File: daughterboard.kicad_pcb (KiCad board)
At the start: 2 copper layers, 72.2 x 85.7 mm, 64 parts, among them J1 MotorA, J10 J, J11 J, J12 J, J13 J, J14 J, J15 J, J16 J, J17 J, J18 J, J19 J, J2 MotorB, J20 J, J21 J, J22 J, J23 J, J24 J, J25 J, J26 J, J27 J, J28 J, J29 J, J3 BARREL_JACK, J30 J, J31 J, J32 J, J33 J, J34 J, J35 J, J36 J, J37 J, J38 J, J39 J, J4 Debug, J40 J, J41 J, J42 J, J43 J, J44 J, J5 QTR-8A, J6 J, J7 J, J8 J, J9 J, SW1 Reset, U1 LD1117S33CTR, U2 TB6612FNG, U3 EFM32G230F128

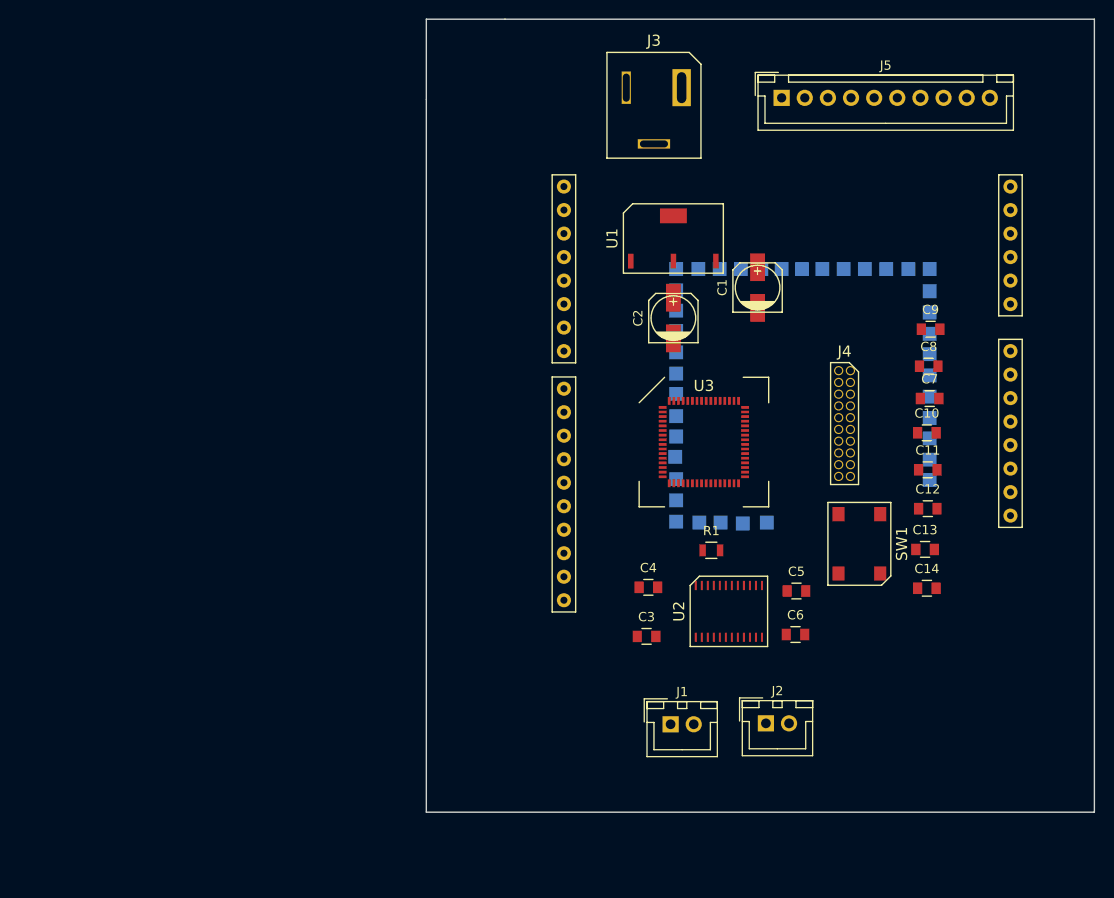
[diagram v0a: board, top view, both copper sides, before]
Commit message: Update PCB to reflect schematic changes
Since we reannotated just about the entire schematic it was easier
to just clear the entire pcb and layout the components again.

Moved the QR8 to the bottom and TB6612 to the top, since it made
more sense wrt the pinout of the EFM32.
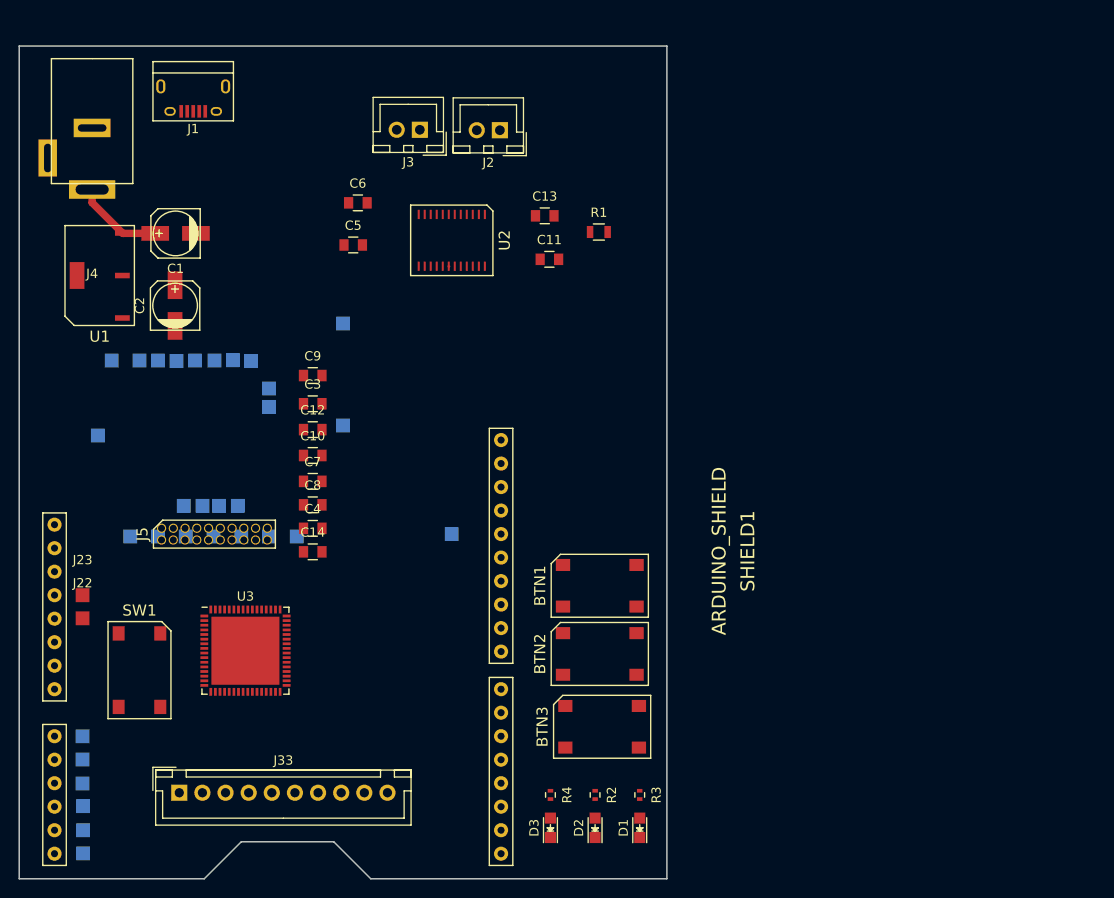
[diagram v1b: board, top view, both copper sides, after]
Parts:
- removed J40, J41, J42, J43, J44: J, Measurement_Points:Measurement_Point_Square-SMD-Pad_Small
- added BTN1: Button, footprints:SW-4, F.Cu at (126.7, 116.3)
- added BTN2: Button, footprints:SW-4, F.Cu at (126.7, 123.7)
- added BTN3: Button, footprints:SW-4, F.Cu at (127.0, 131.6)
- added D1: LED, LEDs:LED_0805, F.Cu at (131.1, 142.5)
- added D2: LED, LEDs:LED_0805, F.Cu at (126.2, 142.5)
- added D3: LED, LEDs:LED_0805, F.Cu at (121.4, 142.5)
- added R2: R, Resistors_SMD:R_0402, F.Cu at (126.2, 138.9)
- added R3: R, Resistors_SMD:R_0402, F.Cu at (131.1, 138.9)
- added R4: R, Resistors_SMD:R_0402, F.Cu at (121.4, 138.9)
- J1: value MotorA -> USB_OTG; footprint Connectors_JST:JST_XH_B02B-XH-A_02x2.50mm_Straight -> Connect:USB_Micro-B
- J2: value MotorB -> MotorA
- J22, J23: moved to F.Cu
- J3: value BARREL_JACK -> MotorB; footprint footprints:BarrelJack -> Connectors_JST:JST_XH_B02B-XH-A_02x2.50mm_Straight
- J33: value J -> QTR-8A; footprint Measurement_Points:Measurement_Point_Square-SMD-Pad_Small -> Connectors_JST:JST_XH_B10B-XH-A_10x2.50mm_Straight; moved to F.Cu
- J4: value Debug -> BARREL_JACK; footprint footprints:SOIC-20 -> footprints:2.1-MM-DC-PWR
- J5: value QTR-8A -> Debug; footprint Connectors_JST:JST_XH_B10B-XH-A_10x2.50mm_Straight -> footprints:SOIC-20
- U3: footprint footprints:QFN64 -> Housings_DFN_QFN:QFN-64-1EP_9x9mm_Pitch0.5mm
- moved J18 108.4 mm to (70.9, 140.2)
- moved J17 107.9 mm to (70.9, 142.8)
- moved J16 107.3 mm to (70.9, 145.2)
- moved J19 105.9 mm to (70.8, 137.7)
- moved J20 103.5 mm to (70.8, 135.1)
- moved J21 101.4 mm to (70.8, 132.6)
- moved J22 95.9 mm to (70.8, 119.8)
- moved J23 94.6 mm to (70.8, 117.3)
- moved J25 89.9 mm to (72.5, 100.1)
- moved J28 89.3 mm to (74.0, 92.0)
- moved J4 86.2 mm to (71.9, 70.1), turned to 180 degrees
- moved J1 85.2 mm to (82.8, 63.5), turned to 180 degrees
- moved J27 84.1 mm to (79.0, 92.0)
- moved J26 81.8 mm to (81.0, 92.0)
- moved J24 79.5 mm to (83.0, 92.0)
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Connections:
- net /ADCO_CH0 renamed Net-(J5-Pad1)
- net /ADCO_CH2 renamed Net-(J5-Pad3)
- net /ADCO_CH4 renamed Net-(J5-Pad5)
- net Net-(C14-Pad1) renamed /EFM32/DCPL
- net Net-(R1-Pad1) renamed /TB6612/STBY
- J1 pad 1: /TB6612/MotorA1 -> +5V
- J1 pad 2: /TB6612/MotorA2 -> Net-(J1-Pad2)
- J10 pad 1: /PE8 -> /EFM32/PB7
- J11 pad 1: /PE9 -> /EFM32/PB8
- J12 pad 1: /PE10 -> Net-(J12-Pad1)
- J13 pad 1: /PE11 -> Net-(J13-Pad1)
- J14 pad 1: /PE12 -> Net-(J14-Pad1)
- J15 pad 1: /PE13 -> Net-(J15-Pad1)
- J16 pad 1: /PF3 -> /AD5
- J17 pad 1: /PF4 -> /AD4
- J18 pad 1: /PF5 -> /AD3
- J19 pad 1: /EFM32/PA9 -> /AD2
- J2 pad 1: /TB6612/MotorB1 -> /TB6612/MotorA1
- J2 pad 2: /TB6612/MotorB2 -> /TB6612/MotorA2
- J20 pad 1: /EFM32/PA10 -> /AD1
- J21 pad 1: /EFM32/PA15 -> /AD0
- J22 pad 1: /EFM32/PB7 -> Net-(J22-Pad1)
- J23 pad 1: /EFM32/PB8 -> Net-(J23-Pad1)
- J24 pad 1: /PB14 -> /EFM32/PE8
- J25 pad 1: /PB13 -> /EFM32/PE9
- J26 pad 1: /PB12 -> /EFM32/PE12
- J27 pad 1: /PB11 -> /EFM32/PE13
- J28 pad 1: Net-(J28-Pad1) -> /EFM32/PE14
- J29 pad 1: Net-(J29-Pad1) -> /EFM32/PE15
- J3 pad 1: +5V -> /TB6612/MotorB2
- J3 pad 2: GND -> /TB6612/MotorB1
- J30 pad 1: Net-(J30-Pad1) -> /EFM32/PF3
- J31 pad 1: Net-(J31-Pad1) -> /EFM32/PF4
- J32 pad 1: /PA0 -> /EFM32/PF5
- J33 pad 1: /PA1 -> /EFM32/ADC0_CH0
- J34 pad 1: /PA2 -> /EFM32/PA5
- J35 pad 1: /PA3 -> /EFM32/PA6
- J36 pad 1: /PA4 -> /EFM32/PB11
- J37 pad 1: /PA5 -> /EFM32/PB12
- J38 pad 1: /PA6 -> /EFM32/PB13
- J39 pad 1: Net-(J39-Pad1) -> /EFM32/PB14
- J4 pad 1: Net-(J4-Pad1) -> +5V
- J4 pad 2: +3V3 -> GND
- J4 pad 3: Net-(J4-Pad3) -> GND
- J5 pad 2: /ADCO_CH1 -> +3V3
- J5 pad 4: /ADCO_CH3 -> GND
- J5 pad 6: /ADCO_CH5 -> GND
- J5 pad 7: /ADCO_CH6 -> /EFM32/PF1
- J5 pad 8: /ADCO_CH7 -> GND
- J5 pad 9: +3V3 -> /EFM32/PF0
- SHIELD1 pad 10: Net-(J28-Pad1) -> Net-(J12-Pad1)
- SHIELD1 pad 11: Net-(J29-Pad1) -> Net-(J13-Pad1)
- SHIELD1 pad 12: Net-(J30-Pad1) -> Net-(J14-Pad1)
- SHIELD1 pad 13: Net-(J31-Pad1) -> Net-(J15-Pad1)
- SHIELD1 pad 2: /PC0 -> /EFM32/PC0
- SHIELD1 pad 3: /PC1 -> /EFM32/PC1
- SHIELD1 pad 3V3: Net-(SHIELD1-Pad3V3) -> Net-(J23-Pad1)
- SHIELD1 pad 4: /PC2 -> /EFM32/PC2
- SHIELD1 pad 5: /PC3 -> /EFM32/PC3
- SHIELD1 pad 5V: Net-(SHIELD1-Pad5V) -> Net-(J22-Pad1)
- SHIELD1 pad 6: /PC4 -> /EFM32/PC4
- SHIELD1 pad 7: /PC5 -> /EFM32/PC5
- SHIELD1 pad 8: /PC6 -> /EFM32/PC6
- SHIELD1 pad 9: /PC7 -> /EFM32/PC7
- SHIELD1 pad A0: (no net) -> /AD0
- SHIELD1 pad A1: (no net) -> /AD1
- SHIELD1 pad A2: (no net) -> /AD2
- SHIELD1 pad A3: (no net) -> /AD3
- SHIELD1 pad VIN: (no net) -> Net-(SHIELD1-PadVIN)
- U2 pad 18: Net-(U2-Pad18) -> GND
- U3 pad 1: /PA0 -> /EFM32/SDA
- U3 pad 2: /PA1 -> /EFM32/SCL
- U3 pad 28: /EFM32/ADCO_CH0 -> /EFM32/ADC0_CH0
- U3 pad 29: /EFM32/ADCO_CH1 -> /EFM32/ADC0_CH1
- U3 pad 3: /PA2 -> /EFM32/PA2
- U3 pad 30: /EFM32/ADCO_CH2 -> /EFM32/ADC0_CH2
- U3 pad 31: /EFM32/ADCO_CH3 -> /EFM32/ADC0_CH3
- U3 pad 32: /EFM32/ADCO_CH4 -> /EFM32/ADC0_CH4
- U3 pad 33: /EFM32/ADCO_CH5 -> /EFM32/ADC0_CH5
- U3 pad 34: /EFM32/ADCO_CH6 -> /EFM32/ADC0_CH6
- U3 pad 35: /EFM32/ADCO_CH7 -> /EFM32/ADC0_CH7
- U3 pad 4: /PA3 -> /EFM32/PA3
- U3 pad 5: /PA4 -> /EFM32/PA4
- U3 pad 58: /EFM32/PE10 -> /EFM32/TX
- U3 pad 59: /EFM32/PE11 -> /EFM32/RX
- U3 pad 6: /PA5 -> /EFM32/PA5
- U3 pad 62: /EFM32/TX -> /EFM32/PE14
- U3 pad 63: /EFM32/RX -> /EFM32/PE15
- U3 pad 7: /PA6 -> /EFM32/PA6
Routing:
- net +5V: track 0.00 -> 9.62 mm
- added copper zone on 3V3, net +3V3
- added copper zone on GND, net GND
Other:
- board size 72.2 x 85.7 mm -> 70 x 90 mm
- copper layers 2 -> 4
- net class Default: clearance 0.25 -> 0.1; trace_width 0.25 -> 0.1
- rule trace_clearance: 0.25 -> 0.1
- rule trace_min: 0.25 -> 0.1

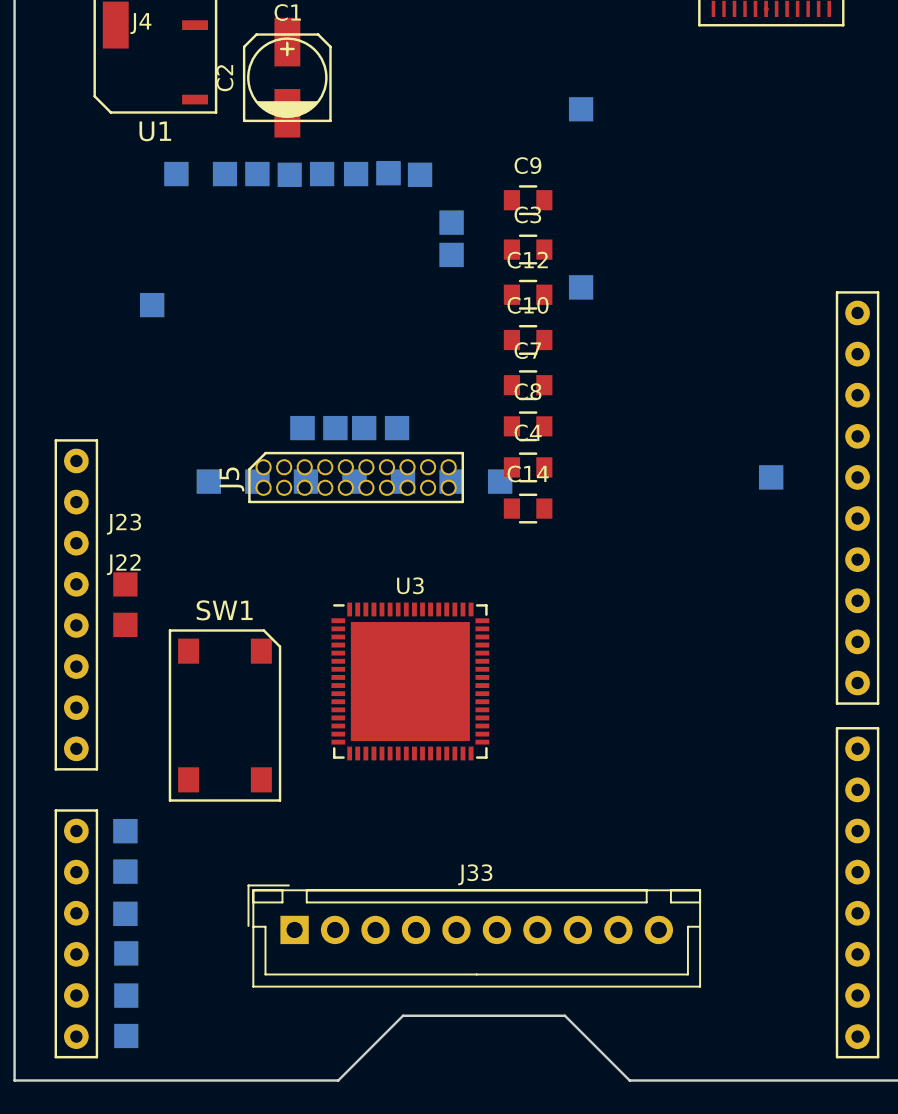
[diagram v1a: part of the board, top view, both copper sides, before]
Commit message: Fix merge conflicts
Trying to merge manually with Kicad is a bad idea.
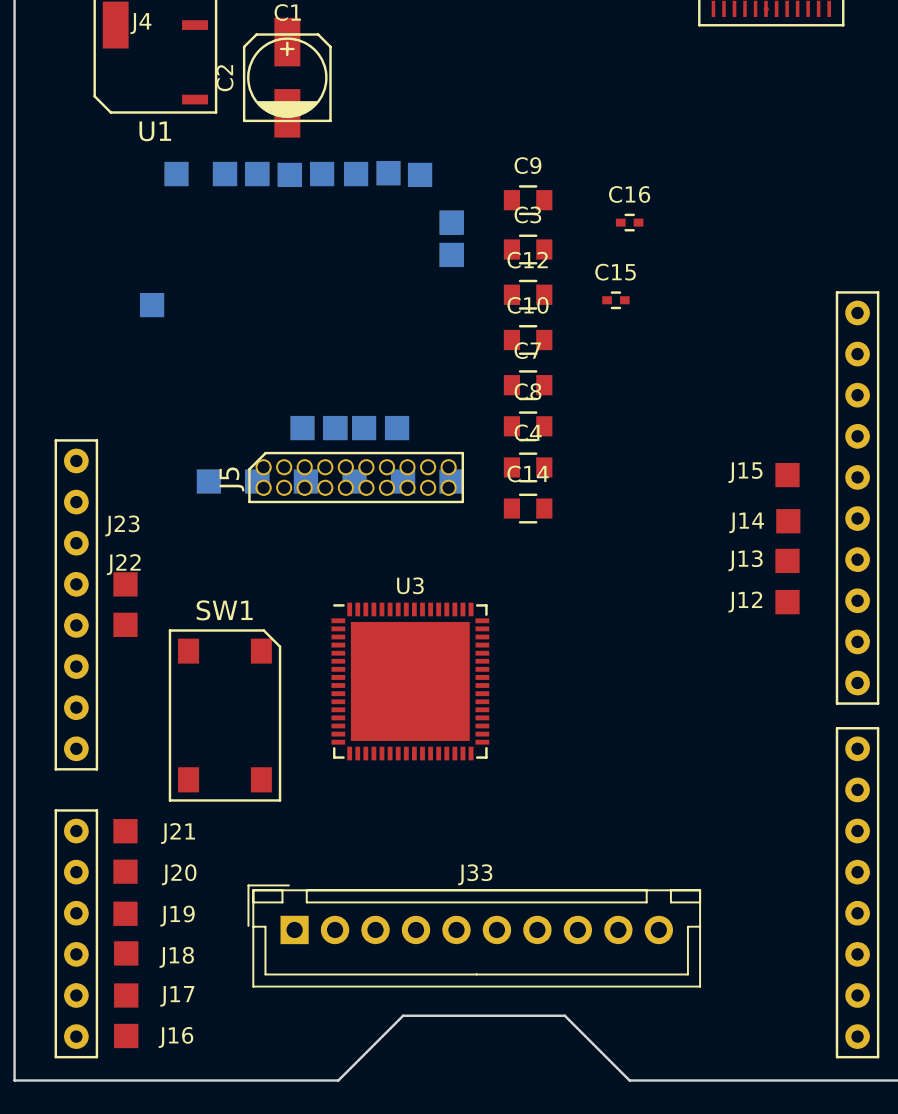
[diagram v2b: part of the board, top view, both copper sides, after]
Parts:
- added C15: 10pF, Capacitors_SMD:C_0402, F.Cu at (101.2, 99.8)
- added C16: 10pF, Capacitors_SMD:C_0402, F.Cu at (102.0, 95.0)
- J12, J13, J14, J15, J16, J17, J18, J19, J20, J21: moved to F.Cu
- moved J12 33.0 mm to (111.8, 118.5)
- moved J14 19.3 mm to (111.8, 113.5)
- moved J13 18.4 mm to (111.8, 115.9)
- moved J15 1.02 mm to (111.8, 110.6)
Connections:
- D1 pad 1: Net-(D1-Pad1) -> GND
- D2 pad 1: Net-(D2-Pad1) -> GND
- D3 pad 1: Net-(D3-Pad1) -> GND
- R2 pad 2: Net-(R2-Pad2) -> Net-(D1-Pad2)
- R3 pad 2: Net-(R3-Pad2) -> Net-(D2-Pad2)
- R4 pad 2: Net-(R4-Pad2) -> Net-(D3-Pad2)

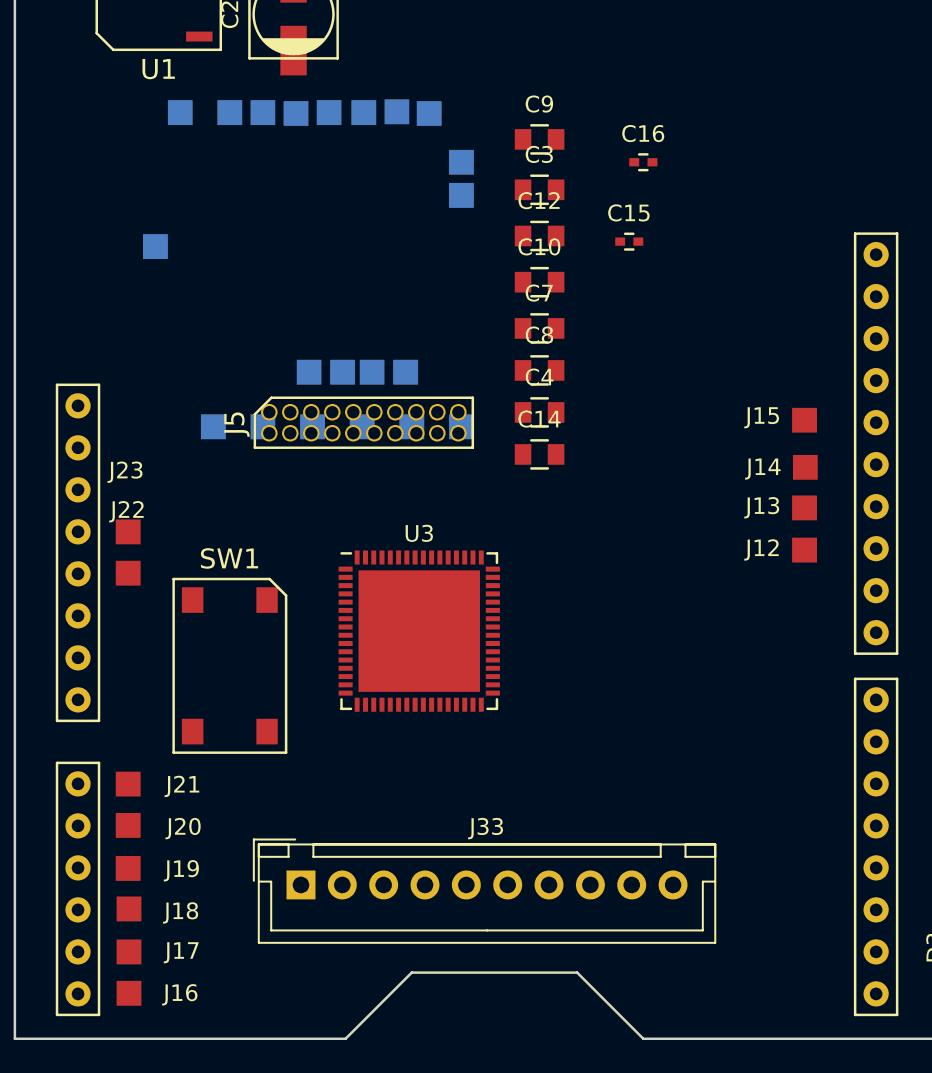
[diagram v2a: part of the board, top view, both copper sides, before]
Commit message: Use round measurement pads
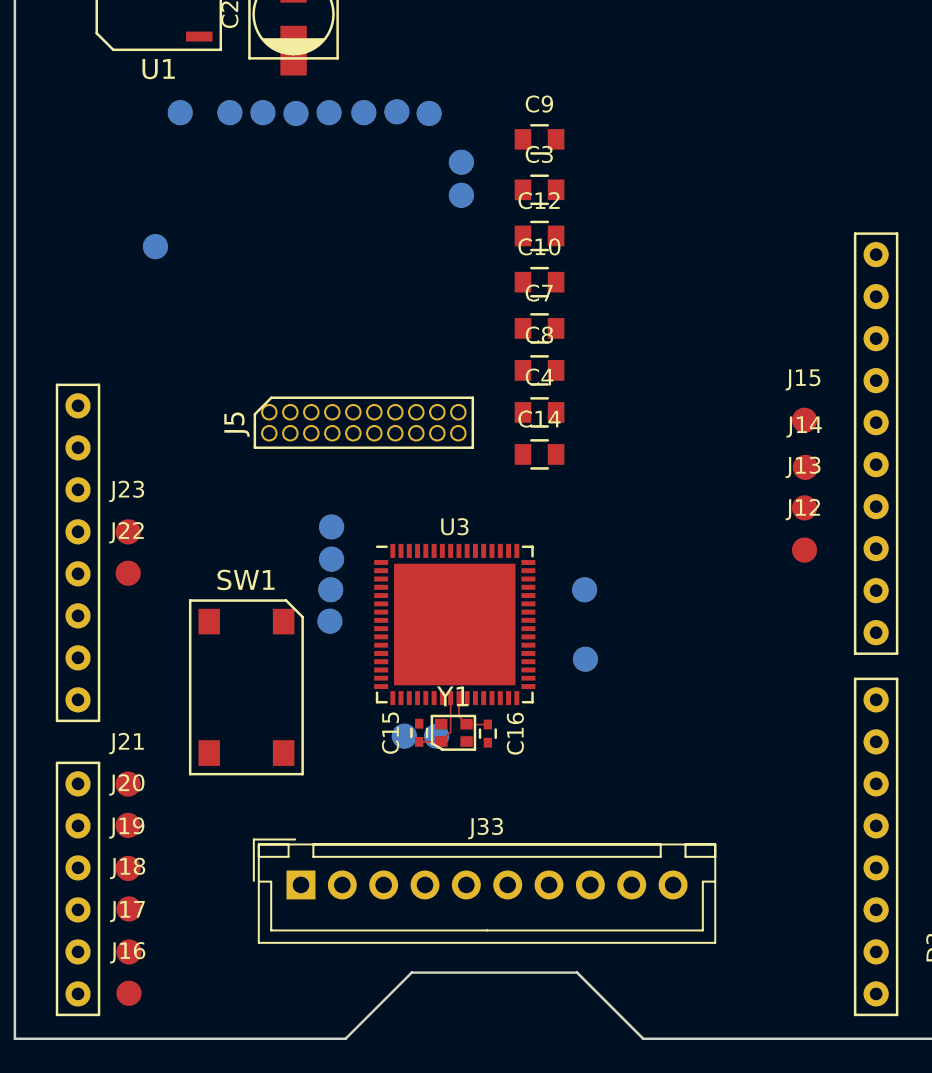
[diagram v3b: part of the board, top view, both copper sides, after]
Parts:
- removed J38, J39: J, Measurement_Points:Measurement_Point_Square-SMD-Pad_Small
- added Y1: Crystal, footprints:ABM11, F.Cu at (90.5, 129.5)
- J10, J11, J12, J13, J14, J15, J16, J17, J18, J19, J20, J21, J22, J23, J24, J25, J26, J27, J28, J29, J30, J31, J32, J34, J35, J36, J37, J6, J7, J8, J9: footprint Measurement_Points:Measurement_Point_Square-SMD-Pad_Small -> Measurement_Points:Measurement_Point_Round-SMD-Pad_Small
- moved C16 35.8 mm to (92.6, 129.6), turned to 270 degrees
- moved C15 32.3 mm to (88.5, 129.5), turned to 90 degrees
- moved J36 22.0 mm to (87.5, 129.7)
- moved J37 21.4 mm to (89.5, 129.7)
- moved J9 17.5 mm to (98.5, 125.0)
- moved J34 15.1 mm to (83.0, 122.8)
- moved J35 13.2 mm to (83.1, 120.8)
- moved J6 12.4 mm to (98.5, 120.8)
- moved J10 11.6 mm to (83.2, 119.0)
- moved J11 10.4 mm to (83.2, 117.0)
- moved U3 2.19 mm to (90.6, 123.0)
- moved SW1 1.64 mm to (78.0, 126.8)
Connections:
- SHIELD1 pad 2: /EFM32/PC0 -> /EFM32/PC5
- SHIELD1 pad 3: /EFM32/PC1 -> /EFM32/PC4
- SHIELD1 pad 4: /EFM32/PC2 -> /EFM32/PC3
- SHIELD1 pad 5: /EFM32/PC3 -> /EFM32/PC2
- SHIELD1 pad 6: /EFM32/PC4 -> /EFM32/PC1
- SHIELD1 pad 7: /EFM32/PC5 -> /EFM32/PC0
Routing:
- net /EFM32/PB13: track 0.00 -> 4.20 mm
- net /EFM32/PB14: track 0.00 -> 3.06 mm
